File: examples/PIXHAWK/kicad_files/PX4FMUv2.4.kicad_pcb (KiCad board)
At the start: 6 copper layers, 70 x 40.5 mm, 354 parts, among them J201 DF13C-6P-1.25V, J202 DF13C-6P-1.25V, J203 DF13C-6P-1.25V, J204 DF13C-6P-1.25V, J301 47346-0001, J302 DF13C-4P-1.25V, J401 DF13C-4P-1.25V, J402 DF13C-3P-1.25V, J403 DF13C-7P-1.25V, J404 DF13C-5P-1.25V, J405 DF13C-4P-1.25V, J601 DF13C-6P-1.25V, J701 DF13C-2P-1.25V, J702 DF13C-3P-1.25V, J801 JST-ZH-3, M3_MOUNT1101 MOUNT-HOLE3.1MM, M3_MOUNT1102 MOUNT-HOLE3.1MM, M3_MOUNT1103 MOUNT-HOLE3.1MM, M3_MOUNT1104 MOUNT-HOLE3.1MM, Q601 MMBT3906LT1SMD, U1001 BQ24313, U1002 MIC5332, U101 STM32F4X7VX, U102 FM25V01, U1101 LTC4417, U1102 NTHD4102PT1G, U1103 NTHD4102PT1G, U1104 NTHD4102PT1G, U201 TXS0108QFN20, U202 TXS0108QFN20, U301 2908-05WB-MG, U302 NUF2042XV6, U401 MAX3051, U501 L3GD20, U502 L3GD20H, U504 LSM303D, U505 MPU-6000, U506 MS5611-01BA, U601 BQ24315, U602 BQ24315, U603 MIC5332, U701 TCA62724FMG, U702 LT3469, U703 LRTB GFTG-T7AW-1+V7A7-29+R5T9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, U801 STM32F10XCXT6, U901 TXS0108QFN20, U902 TXS0108QFN20, U903 74LVC2G240, X101 3.2x2.5 mm / 24 MHz / 15 ppm, X503 0512811094, X801 3.2x2.5 mm / 24 MHz / 15 ppm

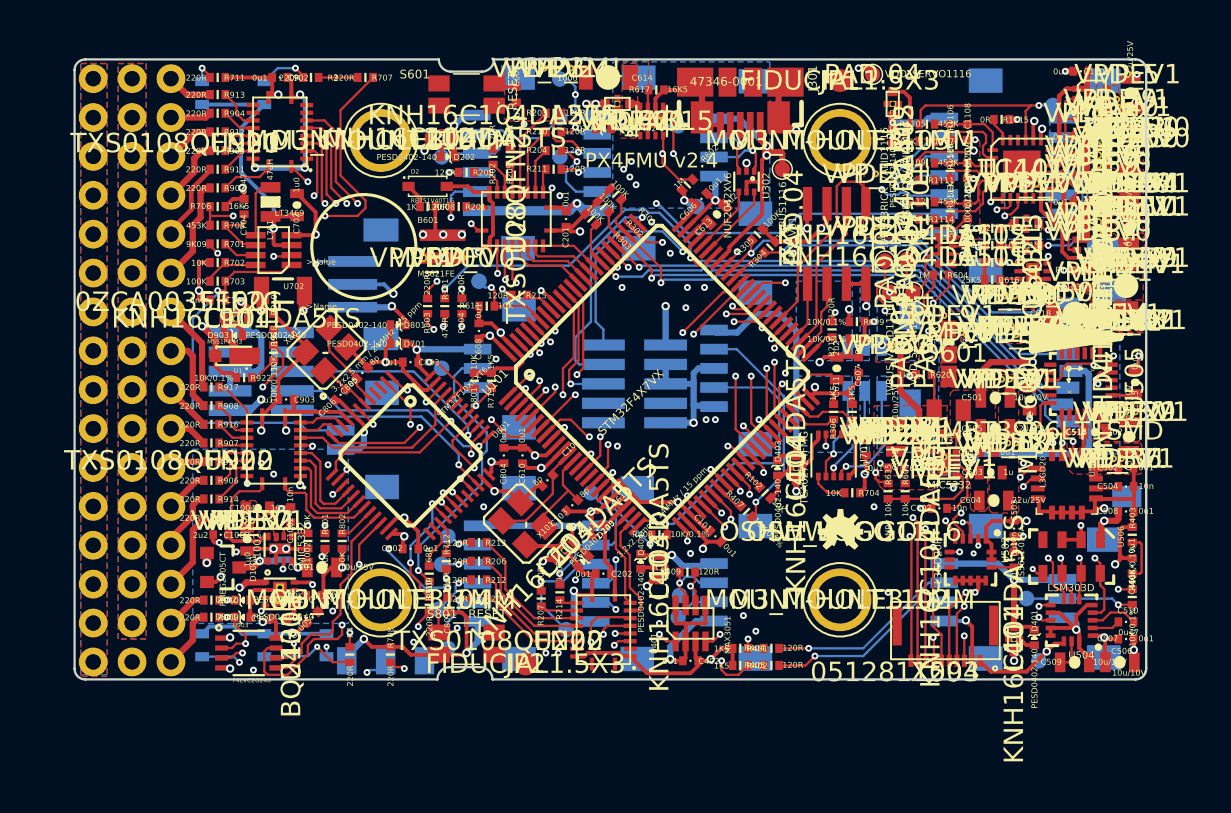
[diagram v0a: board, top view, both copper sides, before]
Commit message: force golbale netnames on, to get around fill/net problem
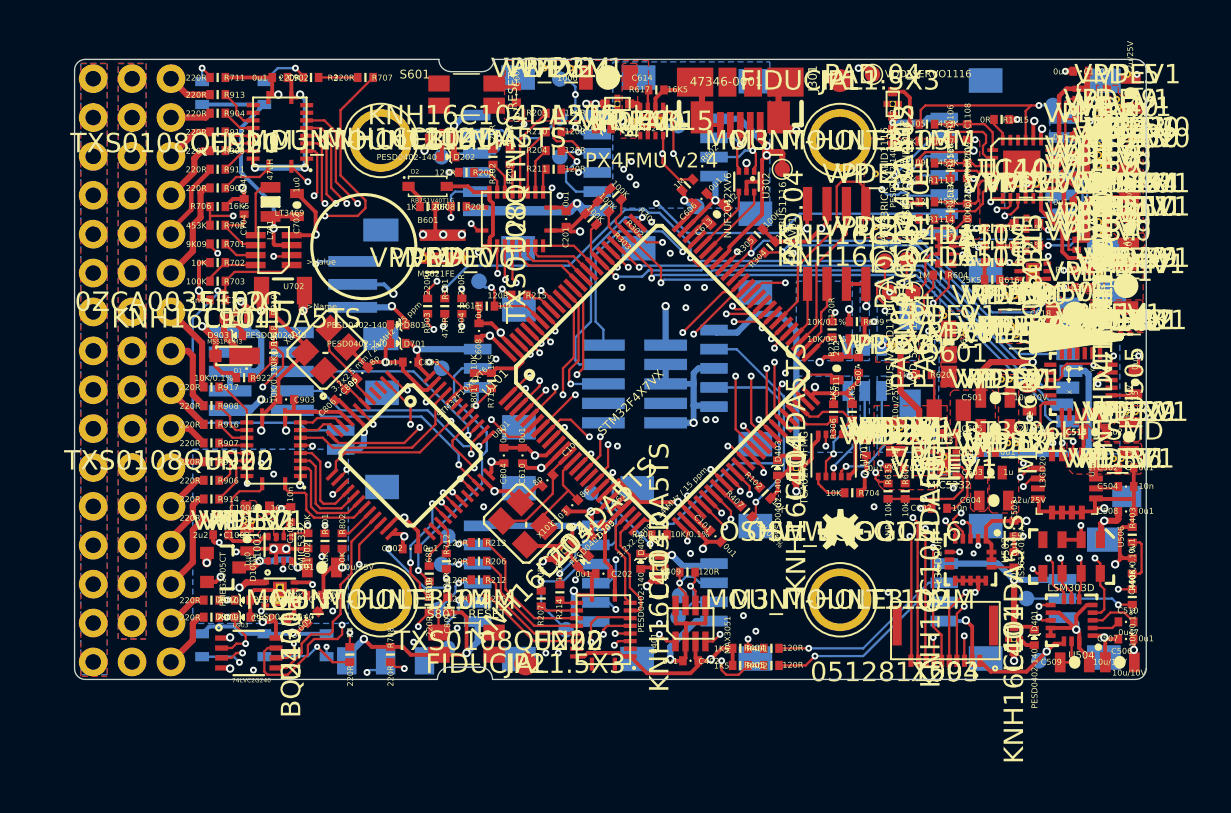
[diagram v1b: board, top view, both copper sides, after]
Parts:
- J901: value ~ -> (none)
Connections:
- net /PX4FMUv2.4_SS_1/!FRAM_CS renamed !FRAM_CS
- net /PX4FMUv2.4_SS_1/FRAM_MISO renamed FRAM_MISO
- net /PX4FMUv2.4_SS_1/FRAM_MOSI renamed FRAM_MOSI
- net /PX4FMUv2.4_SS_1/FRAM_SCK renamed FRAM_SCK
- net /PX4FMUv2.4_SS_1/N$1 renamed N$1
- net /PX4FMUv2.4_SS_1/N$2 renamed N$2
- net /PX4FMUv2.4_SS_1/N$23 renamed N$23
- net /PX4FMUv2.4_SS_1/PB2-BOOT1 renamed PB2-BOOT1
- net /PX4FMUv2.4_SS_10/N$104 renamed N$104
- net /PX4FMUv2.4_SS_10/N$20 renamed N$20
- net /PX4FMUv2.4_SS_10/N$4 renamed N$4
- net /PX4FMUv2.4_SS_10/N$46 renamed N$46
- net /PX4FMUv2.4_SS_11/BATT_CURRENT_SENS_PROT renamed BATT_CURRENT_SENS_PROT
- net /PX4FMUv2.4_SS_11/BATT_VOLTAGE_SENS_PROT renamed BATT_VOLTAGE_SENS_PROT
- net /PX4FMUv2.4_SS_11/N$102 renamed N$102
- net /PX4FMUv2.4_SS_11/N$103 renamed N$103
- net /PX4FMUv2.4_SS_11/N$105 renamed N$105
- net /PX4FMUv2.4_SS_11/N$106 renamed N$106
- net /PX4FMUv2.4_SS_11/N$107 renamed N$107
- net /PX4FMUv2.4_SS_11/N$109 renamed N$109
- net /PX4FMUv2.4_SS_11/N$113 renamed N$113
- net /PX4FMUv2.4_SS_11/N$115 renamed N$115
- net /PX4FMUv2.4_SS_11/N$47 renamed N$47
- net /PX4FMUv2.4_SS_11/N$54 renamed N$54
- net /PX4FMUv2.4_SS_11/N$55 renamed N$55
- net /PX4FMUv2.4_SS_11/N$56 renamed N$56
- net /PX4FMUv2.4_SS_11/N$67 renamed N$67
- net /PX4FMUv2.4_SS_11/N$69 renamed N$69
- net /PX4FMUv2.4_SS_11/N$97 renamed N$97
- net /PX4FMUv2.4_SS_2/N$100 renamed N$100
- net /PX4FMUv2.4_SS_2/N$101 renamed N$101
- net /PX4FMUv2.4_SS_2/N$14 renamed N$14
- net /PX4FMUv2.4_SS_2/N$19 renamed N$19
- net /PX4FMUv2.4_SS_2/N$5 renamed N$5
- net /PX4FMUv2.4_SS_2/N$70 renamed N$70
- net /PX4FMUv2.4_SS_2/N$82 renamed N$82
- net /PX4FMUv2.4_SS_2/N$83 renamed N$83
- net /PX4FMUv2.4_SS_2/N$84 renamed N$84
- net /PX4FMUv2.4_SS_2/N$85 renamed N$85
- net /PX4FMUv2.4_SS_2/N$86 renamed N$86
- net /PX4FMUv2.4_SS_2/N$87 renamed N$87
- net /PX4FMUv2.4_SS_2/N$88 renamed N$88
- net /PX4FMUv2.4_SS_2/N$89 renamed N$89
- net /PX4FMUv2.4_SS_2/N$90 renamed N$90
- net /PX4FMUv2.4_SS_2/N$91 renamed N$91
- net /PX4FMUv2.4_SS_2/N$92 renamed N$92
- net /PX4FMUv2.4_SS_2/N$93 renamed N$93
- net /PX4FMUv2.4_SS_2/N$94 renamed N$94
- net /PX4FMUv2.4_SS_2/SERIAL1_CTS renamed SERIAL1_CTS
- net /PX4FMUv2.4_SS_2/SERIAL1_RTS renamed SERIAL1_RTS
- net /PX4FMUv2.4_SS_2/SERIAL2_CTS renamed SERIAL2_CTS
- net /PX4FMUv2.4_SS_2/SERIAL2_RTS renamed SERIAL2_RTS
- net /PX4FMUv2.4_SS_3/OTG_DM1 renamed OTG_DM1
- net /PX4FMUv2.4_SS_3/OTG_DP1 renamed OTG_DP1
- net /PX4FMUv2.4_SS_4/FMU_AUX_ADC1_PROT renamed FMU_AUX_ADC1_PROT
- net /PX4FMUv2.4_SS_4/FMU_AUX_ADC2_PROT renamed FMU_AUX_ADC2_PROT
- net /PX4FMUv2.4_SS_4/N$33 renamed N$33
- net /PX4FMUv2.4_SS_4/N$37 renamed N$37
- net /PX4FMUv2.4_SS_4/N$41 renamed N$41
- net /PX4FMUv2.4_SS_4/N$42 renamed N$42
- net /PX4FMUv2.4_SS_4/N$48 renamed N$48
- net /PX4FMUv2.4_SS_4/N$98 renamed N$98
- net /PX4FMUv2.4_SS_5/N$10 renamed N$10
- net /PX4FMUv2.4_SS_5/N$17 renamed N$17
- net /PX4FMUv2.4_SS_5/N$30 renamed N$30
- net /PX4FMUv2.4_SS_5/N$35 renamed N$35
- net /PX4FMUv2.4_SS_5/N$50 renamed N$50
- net /PX4FMUv2.4_SS_5/N$51 renamed N$51
- net /PX4FMUv2.4_SS_5/N$6 renamed N$6
- net /PX4FMUv2.4_SS_6/N$11 renamed N$11
- net /PX4FMUv2.4_SS_6/N$12 renamed N$12
- net /PX4FMUv2.4_SS_6/N$21 renamed N$21
- net /PX4FMUv2.4_SS_6/N$34 renamed N$34
- net /PX4FMUv2.4_SS_6/N$8 renamed N$8
- net /PX4FMUv2.4_SS_6/N$80 renamed N$80
- net /PX4FMUv2.4_SS_6/N$81 renamed N$81
- net /PX4FMUv2.4_SS_6/N$96 renamed N$96
- net /PX4FMUv2.4_SS_7/N$13 renamed N$13
- net /PX4FMUv2.4_SS_7/N$24 renamed N$24
- net /PX4FMUv2.4_SS_7/N$25 renamed N$25
- net /PX4FMUv2.4_SS_7/N$26 renamed N$26
- net /PX4FMUv2.4_SS_7/N$27 renamed N$27
- net /PX4FMUv2.4_SS_7/N$28 renamed N$28
- net /PX4FMUv2.4_SS_7/N$29 renamed N$29
- net /PX4FMUv2.4_SS_7/N$32 renamed N$32
- net /PX4FMUv2.4_SS_7/N$36 renamed N$36
- net /PX4FMUv2.4_SS_7/N$39 renamed N$39
- net /PX4FMUv2.4_SS_7/N$40 renamed N$40
- net /PX4FMUv2.4_SS_7/N$57 renamed N$57
- net /PX4FMUv2.4_SS_7/N$7 renamed N$7
- net /PX4FMUv2.4_SS_7/N$9 renamed N$9
- net /PX4FMUv2.4_SS_7/N$95 renamed N$95
- net /PX4FMUv2.4_SS_8/IO-BOOT1 renamed IO-BOOT1
- net /PX4FMUv2.4_SS_8/IO-SWCLK renamed IO-SWCLK
- net /PX4FMUv2.4_SS_8/IO-SWDIO renamed IO-SWDIO
- net /PX4FMUv2.4_SS_8/IO-SWO renamed IO-SWO
- net /PX4FMUv2.4_SS_8/IO-USART1_RX renamed IO-USART1_RX
- net /PX4FMUv2.4_SS_8/N$15 renamed N$15
- net /PX4FMUv2.4_SS_8/N$16 renamed N$16
- net /PX4FMUv2.4_SS_8/N$18 renamed N$18
- net /PX4FMUv2.4_SS_8/N$22 renamed N$22
- net /PX4FMUv2.4_SS_9/FMU-CH1-PROT renamed FMU-CH1-PROT
- net /PX4FMUv2.4_SS_9/FMU-CH6-PROT renamed FMU-CH6-PROT
- net /PX4FMUv2.4_SS_9/IO-CH1-PROT renamed IO-CH1-PROT
- net /PX4FMUv2.4_SS_9/IO-CH8-PROT renamed IO-CH8-PROT
- net /PX4FMUv2.4_SS_9/N$3 renamed N$3
- net /PX4FMUv2.4_SS_9/N$31 renamed N$31
- net /PX4FMUv2.4_SS_9/N$38 renamed N$38
- net /PX4FMUv2.4_SS_9/N$43 renamed N$43
- net /PX4FMUv2.4_SS_9/N$44 renamed N$44
- net /PX4FMUv2.4_SS_9/N$45 renamed N$45
- net /PX4FMUv2.4_SS_9/N$49 renamed N$49
- net /PX4FMUv2.4_SS_9/N$53 renamed N$53
- net /PX4FMUv2.4_SS_9/N$58 renamed N$58
- net /PX4FMUv2.4_SS_9/N$59 renamed N$59
- net /PX4FMUv2.4_SS_9/N$60 renamed N$60
- net /PX4FMUv2.4_SS_9/N$61 renamed N$61
- net /PX4FMUv2.4_SS_9/N$62 renamed N$62
- net /PX4FMUv2.4_SS_9/N$63 renamed N$63
- net /PX4FMUv2.4_SS_9/N$64 renamed N$64
- net /PX4FMUv2.4_SS_9/N$65 renamed N$65
- net /PX4FMUv2.4_SS_9/N$66 renamed N$66
- net /PX4FMUv2.4_SS_9/N$68 renamed N$68
- net /PX4FMUv2.4_SS_9/N$71 renamed N$71
- net /PX4FMUv2.4_SS_9/N$72 renamed N$72
- net /PX4FMUv2.4_SS_9/N$73 renamed N$73
- net /PX4FMUv2.4_SS_9/N$74 renamed N$74
- net /PX4FMUv2.4_SS_9/N$75 renamed N$75
- net /PX4FMUv2.4_SS_9/N$77 renamed N$77
- net /PX4FMUv2.4_SS_9/N$78 renamed N$78
- net /PX4FMUv2.4_SS_9/N$79 renamed N$79
- net /PX4FMUv2.4_SS_9/N$99 renamed N$99
- net /PX4FMUv2.4_SS_9/PPM-SBUS-PROT renamed PPM-SBUS-PROT
- C601 pad P$1: /PX4FMUv2.4_SS_6/FMU-VDD_5V5 -> FMU-VDD_5V5
- C615 pad P$1: /PX4FMUv2.4_SS_6/FMU-VDD_5V5 -> FMU-VDD_5V5
- D1 pad ANOD: VDD_SERVO -> (no net)
- D1 pad CATH: /PX4FMUv2.4_SS_9/N$110 -> (no net)
- D903 pad C: /PX4FMUv2.4_SS_9/N$110 -> N$110
- J301 pad ID: Net-(J301-PadID) -> (no net)
- JX301 pad 10: Net-(JX301-Pad10) -> (no net)
- JX301 pad 8: Net-(JX301-Pad8) -> (no net)
- JX802 pad 10: Net-(JX802-Pad10) -> (no net)
- JX802 pad 8: Net-(JX802-Pad8) -> (no net)
- L603 pad P$2: /PX4FMUv2.4_SS_6/FMU-VDD_5V5 -> FMU-VDD_5V5
- L901 pad P$1: /PX4FMUv2.4_SS_9/N$110 -> N$110
- R603 pad P$1: /PX4FMUv2.4_SS_6/FMU-VDD_5V5 -> FMU-VDD_5V5
- U101 pad 16: Net-(U101-Pad16) -> (no net)
- U1101 pad P$11: Net-(U1101-PadP$11) -> (no net)
- U1101 pad P$22: Net-(U1101-PadP$22) -> (no net)
- U1101 pad P$23: Net-(U1101-PadP$23) -> (no net)
- U202 pad 1: Net-(U202-Pad1) -> (no net)
- U202 pad 18: Net-(U202-Pad18) -> (no net)
- U202 pad 20: Net-(U202-Pad20) -> (no net)
- U202 pad 3: Net-(U202-Pad3) -> (no net)
- U501 pad 7: Net-(U501-Pad7) -> (no net)
- U502 pad 7: Net-(U502-Pad7) -> (no net)
- U502 pad 8: Net-(U502-Pad8) -> (no net)
- U505 pad 11: Net-(U505-Pad11) -> (no net)
- U505 pad 14: Net-(U505-Pad14) -> (no net)
- U505 pad 15: Net-(U505-Pad15) -> (no net)
- U505 pad 16: Net-(U505-Pad16) -> (no net)
- U505 pad 17: Net-(U505-Pad17) -> (no net)
- U505 pad 19: Net-(U505-Pad19) -> (no net)
- U505 pad 2: Net-(U505-Pad2) -> (no net)
- U505 pad 21: Net-(U505-Pad21) -> (no net)
- U505 pad 22: Net-(U505-Pad22) -> (no net)
- U505 pad 3: Net-(U505-Pad3) -> (no net)
- U505 pad 4: Net-(U505-Pad4) -> (no net)
- U505 pad 5: Net-(U505-Pad5) -> (no net)
- U505 pad 6: Net-(U505-Pad6) -> (no net)
- U505 pad 7: Net-(U505-Pad7) -> (no net)
- U506 pad 4: Net-(U506-Pad4) -> (no net)
- U603 pad 1: /PX4FMUv2.4_SS_6/FMU-VDD_5V5 -> FMU-VDD_5V5
- U603 pad 4: /PX4FMUv2.4_SS_6/FMU-VDD_5V5 -> FMU-VDD_5V5
- U701 pad 7: /PX4FMUv2.4_SS_7/RGB_LED_14 -> RGB_LED_14
- U701 pad 8: /PX4FMUv2.4_SS_7/RGB_LED_4 -> RGB_LED_4
- U701 pad 9: /PX4FMUv2.4_SS_7/RGB_LED_3 -> RGB_LED_3
- U703 pad C1: /PX4FMUv2.4_SS_7/RGB_LED_3 -> RGB_LED_3
- U703 pad C2: /PX4FMUv2.4_SS_7/RGB_LED_4 -> RGB_LED_4
- U703 pad C3: /PX4FMUv2.4_SS_7/RGB_LED_14 -> RGB_LED_14
- U801 pad 25: Net-(U801-Pad25) -> (no net)
- U801 pad 3: Net-(U801-Pad3) -> (no net)
- U801 pad 32: Net-(U801-Pad32) -> (no net)
- U801 pad 4: Net-(U801-Pad4) -> (no net)
- U801 pad 42: Net-(U801-Pad42) -> (no net)
- U801 pad 43: Net-(U801-Pad43) -> (no net)
- U901 pad 12: Net-(U901-Pad12) -> (no net)
- U901 pad 13: Net-(U901-Pad13) -> (no net)
- U901 pad 8: Net-(U901-Pad8) -> (no net)
- U901 pad 9: Net-(U901-Pad9) -> (no net)
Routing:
- net RGB_LED_3: track 0.00 -> 7.58 mm, vias 0 -> 1
- net /PX4FMUv2.4_SS_7/RGB_LED_3: track 7.58 -> 0.00 mm, vias 1 -> 0
- net RGB_LED_4: track 0.00 -> 6.43 mm, vias 0 -> 1
- net /PX4FMUv2.4_SS_7/RGB_LED_4: track 6.43 -> 0.00 mm, vias 1 -> 0
- net RGB_LED_14: track 0.00 -> 6.18 mm, vias 0 -> 1
- net /PX4FMUv2.4_SS_7/RGB_LED_14: track 6.18 -> 0.00 mm, vias 1 -> 0
- net N$110: track 0.00 -> 2.99 mm
- net /PX4FMUv2.4_SS_9/N$110: track 2.99 -> 0.00 mm
- added copper zone on F.Cu, net N$80
- removed copper zone on F.Cu, net N$80 (its old number)
